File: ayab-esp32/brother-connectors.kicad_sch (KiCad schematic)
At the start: 16 parts, among them J401 900.965.CK35 SOLENOIDS A, J402 900.965.CK35 SOLENOIDS B, J403 910.950 SOLENOIDS A, J404 910.950 SOLENOIDS B, J405 910.950 ENCODERS EOL R, J406 930.940 SOLENOIDS A, J407 930.940 SOLENOIDS B, J408 910.950 EOL L, J409 930.940 EOL R, J410 930.940 ENCODERS, J411 900.965 EOL L, J412 900.965 EOL R, J413 900.965 ENCODERS, J414 930.940 EOL L

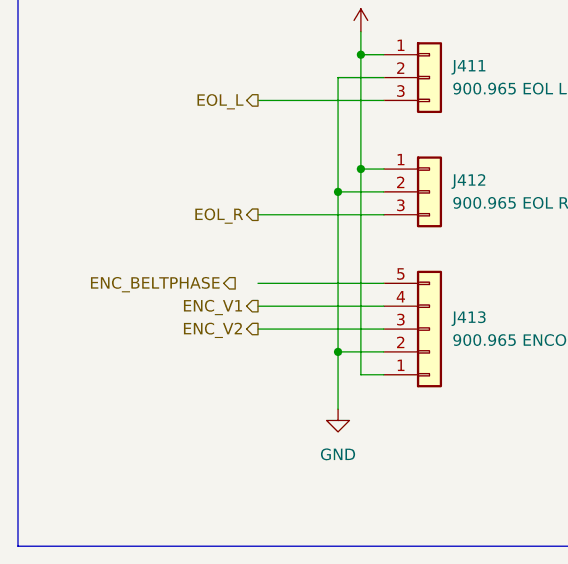
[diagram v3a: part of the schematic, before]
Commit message: review ZVD P-ch MOSFET and resistors
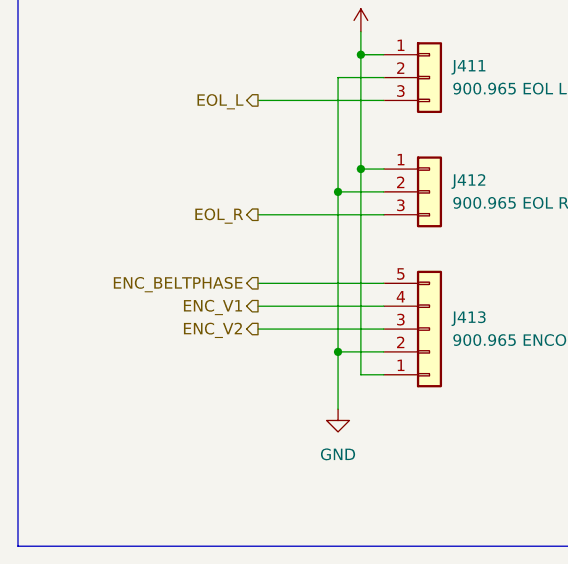
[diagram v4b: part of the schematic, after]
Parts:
- J401, J403, J405, J406: symbol Library:Conn_01x10 -> ayab-lib:Conn_01x10
- J402, J404, J407: symbol Library:Conn_01x08 -> ayab-lib:Conn_01x08
- J408, J409, J411, J412, J414: symbol Library:Conn_01x03 -> ayab-lib:Conn_01x03
- J410, J413: symbol Library:Conn_01x05 -> ayab-lib:Conn_01x05
- TP401, TP402: symbol Library:TestPoint -> ayab-lib:TestPoint
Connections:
- net ENC_BELTPHASE: now also J413.5 (Pin_5)
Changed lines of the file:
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@@
     (effects (font (size 1.27 1.27)) (justify right))
   )
-  (hierarchical_label "ENC_BELTPHASE" (shape output) (at 41.91 130.81 180) (fields_autoplaced)
+  (hierarchical_label "ENC_BELTPHASE" (shape output) (at 44.45 130.81 180) (fields_autoplaced)
     (effects (font (size 1.27 1.27)) (justify right))
   )
@@
     )
   )
-  (symbol (lib_id "Library:Conn_01x03") (at 242.57 110.49 0) (unit 1)
+  (symbol (lib_id "ayab-lib:Conn_01x03") (at 242.57 110.49 0) (unit 1)
     (in_bom yes) (on_board yes) (dnp no) (fields_autoplaced)
     (property "Reference" "J414" (at 245.11 109.22 0)
@@
     )
   )
-  (symbol (lib_id "Library:Conn_01x05") (at 63.5 135.89 0) (mirror x) (unit 1)
+  (symbol (lib_id "ayab-lib:Conn_01x05") (at 63.5 135.89 0) (mirror x) (unit 1)
     (in_bom yes) (on_board yes) (dnp no)
     (property "Reference" "J413" (at 66.04 134.62 0)
@@
     )
   )
-  (symbol (lib_id "Library:Conn_01x03") (at 63.5 107.95 0) (unit 1)
+  (symbol (lib_id "ayab-lib:Conn_01x03") (at 63.5 107.95 0) (unit 1)
     (in_bom yes) (on_board yes) (dnp no) (fields_autoplaced)
     (property "Reference" "J411" (at 66.04 106.68 0)
@@
     )
   )
-  (symbol (lib_id "Library:TestPoint") (at 133.35 118.11 90) (unit 1)
+  (symbol (lib_id "ayab-lib:TestPoint") (at 133.35 118.11 90) (unit 1)
     (in_bom no) (on_board yes) (dnp no)
     (property "Reference" "TP402" (at 123.19 118.11 90)
@@
     )
   )
-  (symbol (lib_id "Library:Conn_01x03") (at 152.4 107.95 0) (unit 1)
+  (symbol (lib_id "ayab-lib:Conn_01x03") (at 152.4 107.95 0) (unit 1)
     (in_bom yes) (on_board yes) (dnp no) (fields_autoplaced)
     (property "Reference" "J408" (at 154.94 106.68 0)
@@
     )
   )
-  (symbol (lib_id "Library:Conn_01x08") (at 152.4 77.47 0) (mirror x) (unit 1)
+  (symbol (lib_id "ayab-lib:Conn_01x08") (at 152.4 77.47 0) (mirror x) (unit 1)
     (in_bom yes) (on_board yes) (dnp no)
     (property "Reference" "J404" (at 154.94 74.93 0)
@@
     )
   )
-  (symbol (lib_id "Library:Conn_01x10") (at 242.57 52.07 0) (mirror x) (unit 1)
+  (symbol (lib_id "ayab-lib:Conn_01x10") (at 242.57 52.07 0) (mirror x) (unit 1)
     (in_bom yes) (on_board yes) (dnp no)
     (property "Reference" "J406" (at 245.11 49.53 0)
@@
     )
   )
-  (symbol (lib_id "Library:TestPoint") (at 133.35 120.65 90) (unit 1)
+  (symbol (lib_id "ayab-lib:TestPoint") (at 133.35 120.65 90) (unit 1)
     (in_bom no) (on_board yes) (dnp no)
     (property "Reference" "TP401" (at 123.19 120.65 90)
@@
     )
   )
-  (symbol (lib_id "Library:Conn_01x10") (at 152.4 49.53 0) (mirror x) (unit 1)
+  (symbol (lib_id "ayab-lib:Conn_01x10") (at 152.4 49.53 0) (mirror x) (unit 1)
     (in_bom yes) (on_board yes) (dnp no)
     (property "Reference" "J403" (at 154.94 46.99 0)
@@
     )
   )
-  (symbol (lib_id "Library:Conn_01x08") (at 63.5 77.47 0) (mirror x) (unit 1)
+  (symbol (lib_id "ayab-lib:Conn_01x08") (at 63.5 77.47 0) (mirror x) (unit 1)
     (in_bom yes) (on_board yes) (dnp no)
     (property "Reference" "J402" (at 66.04 74.93 0)
@@
     )
   )
-  (symbol (lib_id "Library:Conn_01x08") (at 242.57 80.01 0) (mirror x) (unit 1)
+  (symbol (lib_id "ayab-lib:Conn_01x08") (at 242.57 80.01 0) (mirror x) (unit 1)
     (in_bom yes) (on_board yes) (dnp no)
     (property "Reference" "J407" (at 245.11 77.47 0)
@@
     )
   )
-  (symbol (lib_id "Library:Conn_01x10") (at 152.4 130.81 0) (mirror x) (unit 1)
+  (symbol (lib_id "ayab-lib:Conn_01x10") (at 152.4 130.81 0) (mirror x) (unit 1)
     (in_bom yes) (on_board yes) (dnp no)
     (property "Reference" "J405" (at 154.94 138.43 0)
@@
     )
   )
-  (symbol (lib_id "Library:Conn_01x10") (at 63.5 49.53 0) (mirror x) (unit 1)
+  (symbol (lib_id "ayab-lib:Conn_01x10") (at 63.5 49.53 0) (mirror x) (unit 1)
     (in_bom yes) (on_board yes) (dnp no)
     (property "Reference" "J401" (at 66.04 46.99 0)
@@
     )
   )
-  (symbol (lib_id "Library:Conn_01x05") (at 242.57 138.43 0) (mirror x) (unit 1)
+  (symbol (lib_id "ayab-lib:Conn_01x05") (at 242.57 138.43 0) (mirror x) (unit 1)
     (in_bom yes) (on_board yes) (dnp no)
     (property "Reference" "J410" (at 245.11 137.16 0)
@@
     )
   )
-  (symbol (lib_id "Library:Conn_01x03") (at 63.5 120.65 0) (unit 1)
+  (symbol (lib_id "ayab-lib:Conn_01x03") (at 63.5 120.65 0) (unit 1)
     (in_bom yes) (on_board yes) (dnp no) (fields_autoplaced)
     (property "Reference" "J412" (at 66.04 119.38 0)
@@
     )
   )
-  (symbol (lib_id "Library:Conn_01x03") (at 242.57 123.19 0) (unit 1)
+  (symbol (lib_id "ayab-lib:Conn_01x03") (at 242.57 123.19 0) (unit 1)
     (in_bom yes) (on_board yes) (dnp no) (fields_autoplaced)
     (property "Reference" "J409" (at 245.11 121.92 0)

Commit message: first draft layout DRC clean
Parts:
- J401: footprint Library:CONN-TH_CNJMA2004WV-10P -> Library:530141010
- J402: footprint Library:CONN-TH_A2004WV-8P -> Library:530140810
- J403, J405: footprint (none) -> Library:HNC2-2.5P-10DS
- J404: footprint (none) -> Library:HNC2-2.5P-8DS
- J406: footprint Connector_JST:JST_XH_B10B-XH-A_1x10_P2.50mm_Vertical -> Library:SHDR10W70P0X250_1X10_2740X490X590P
- J407: footprint easyeda2kicad:CONN-TH_A2506WV-08P -> Library:SHDR8W65P0X250_1X8_2240X490X610P
- J408: footprint Connector_JST:JST_XH_B3B-XH-A_1x03_P2.50mm_Vertical -> Library:HNC2-2.5P-3DS
- J413: footprint Library:CONN-TH_A2004WV-5P -> Library:530140510
- TP401, TP402: footprint TestPoint:TestPoint_Pad_D2.0mm -> TestPoint:TestPoint_Pad_D1.0mm
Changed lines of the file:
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@@
       (effects (font (size 1.27 1.27)) (justify left))
     )
-    (property "Footprint" "Library:CONN-TH_A2004WV-5P" (at 63.5 135.89 0)
+    (property "Footprint" "Library:530140510" (at 63.5 135.89 0)
       (effects (font (size 1.27 1.27)) hide)
     )
@@
       (effects (font (size 1.27 1.27)) (justify left))
     )
-    (property "Footprint" "TestPoint:TestPoint_Pad_D2.0mm" (at 133.35 113.03 0)
+    (property "Footprint" "TestPoint:TestPoint_Pad_D1.0mm" (at 133.35 113.03 0)
       (effects (font (size 1.27 1.27)) hide)
     )
@@
       (effects (font (size 1.27 1.27)) (justify left))
     )
-    (property "Footprint" "Connector_JST:JST_XH_B3B-XH-A_1x03_P2.50mm_Vertical" (at 152.4 107.95 0)
+    (property "Footprint" "Library:HNC2-2.5P-3DS" (at 152.4 107.95 0)
       (effects (font (size 1.27 1.27)) hide)
     )
@@
       (effects (font (size 1.27 1.27)) (justify left))
     )
-    (property "Footprint" "" (at 152.4 77.47 0)
+    (property "Footprint" "Library:HNC2-2.5P-8DS" (at 152.4 77.47 0)
       (effects (font (size 1.27 1.27)) hide)
     )
@@
       (effects (font (size 1.27 1.27)) (justify left))
     )
-    (property "Footprint" "Connector_JST:JST_XH_B10B-XH-A_1x10_P2.50mm_Vertical" (at 242.57 52.07 0)
+    (property "Footprint" "Library:SHDR10W70P0X250_1X10_2740X490X590P" (at 242.57 52.07 0)
       (effects (font (size 1.27 1.27)) hide)
     )
@@
       (effects (font (size 1.27 1.27)) (justify left))
     )
-    (property "Footprint" "TestPoint:TestPoint_Pad_D2.0mm" (at 133.35 115.57 0)
+    (property "Footprint" "TestPoint:TestPoint_Pad_D1.0mm" (at 133.35 115.57 0)
       (effects (font (size 1.27 1.27)) hide)
     )
@@
       (effects (font (size 1.27 1.27)) (justify left))
     )
-    (property "Footprint" "" (at 152.4 49.53 0)
+    (property "Footprint" "Library:HNC2-2.5P-10DS" (at 152.4 49.53 0)
       (effects (font (size 1.27 1.27)) hide)
     )
@@
       (effects (font (size 1.27 1.27)) (justify left))
     )
-    (property "Footprint" "Library:CONN-TH_A2004WV-8P" (at 63.5 77.47 0)
+    (property "Footprint" "Library:530140810" (at 63.5 77.47 0)
       (effects (font (size 1.27 1.27)) hide)
     )
@@
       (effects (font (size 1.27 1.27)) (justify left))
     )
-    (property "Footprint" "easyeda2kicad:CONN-TH_A2506WV-08P" (at 242.57 80.01 0)
+    (property "Footprint" "Library:SHDR8W65P0X250_1X8_2240X490X610P" (at 242.57 80.01 0)
       (effects (font (size 1.27 1.27)) hide)
     )
@@
       (effects (font (size 1.27 1.27)) (justify left))
     )
-    (property "Footprint" "" (at 152.4 130.81 0)
+    (property "Footprint" "Library:HNC2-2.5P-10DS" (at 152.4 130.81 0)
       (effects (font (size 1.27 1.27)) hide)
     )
@@
       (effects (font (size 1.27 1.27)) (justify left))
     )
-    (property "Footprint" "Library:CONN-TH_CNJMA2004WV-10P" (at 63.5 49.53 0)
-      (effects (font (size 1.27 1.27)) hide)
-    )
+    (property "Footprint" "Library:530141010" (at 63.5 49.53 0)
+      (effects (font (size 1.27 1.27)) hide)
+    )

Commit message: add mouser parts list
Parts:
- J401: Mouser PN (none) -> 538-53014-1010
- J402: Mouser PN (none) -> 538-53014-0810
- J403, J405: Mouser PN (none) -> 798-HNC22.5P10DS55
- J404: Mouser PN (none) -> 798-HNC2-2.5P-8DS55
- J406: Mouser PN (none) -> 538-22-03-5105
- J407: Mouser PN (none) -> 538-22-03-5085
- J408: Mouser PN (none) -> 798-HNC2-2.5P-3DS55
- J409, J414: Mouser PN (none) -> 538-22-03-5035
- J410: Mouser PN (none) -> 538-22-03-5055
- J411, J412: Mouser PN (none) -> 538-53014-0310
- J413: Mouser PN (none) -> 538-53014-0510

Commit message: clean ERC DRC, fix library paths
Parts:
- J409, J414: footprint easyeda2kicad:CONN-TH_3P-P2.50_X2564WV-03-N0SN -> Library:CONN-TH_3P-P2.50_X2564WV-03-N0SN
- J410: footprint easyeda2kicad:CONN-TH_X2564WV-05-N0SN -> Library:CONN-TH_X2564WV-05-N0SN
